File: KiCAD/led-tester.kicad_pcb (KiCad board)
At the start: 2 copper layers, 53.3 x 30.5 mm, 25 parts, among them IC401 ATTINY1634, P101 CONN_01X02, P102 CONN_01X02, P103 CONN_01X03, P104 CONN_02X03, P401 CONN_02X07, SW301 SWITCH_SPDT, U201 LM317L, U301 MCP1702

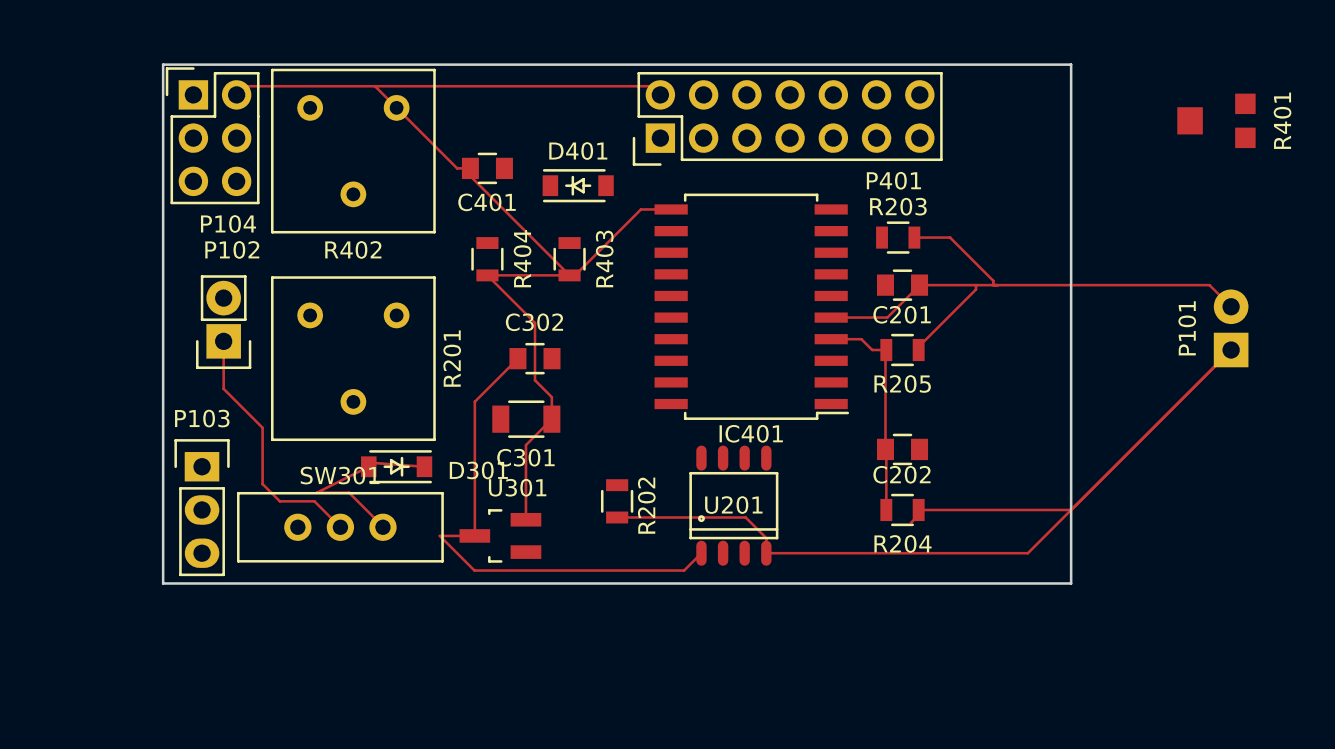
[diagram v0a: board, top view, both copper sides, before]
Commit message: switching back to an ATTiny84 or ATTiny84A
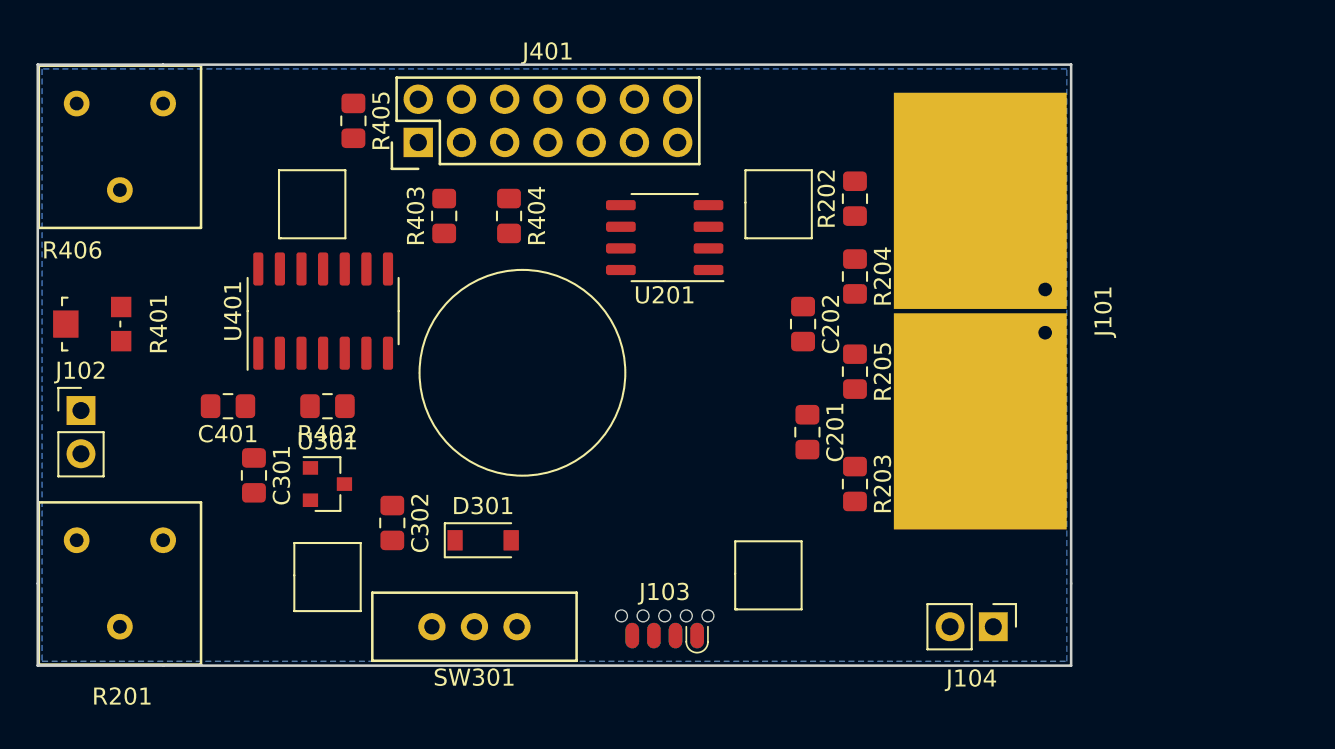
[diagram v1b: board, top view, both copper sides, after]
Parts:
- removed D401: Schottky, Diodes_SMD:SOD-123
- removed IC401: ATTINY1634, led-tester:SOIC-20_7.5x12.8mm_Pitch1.27mm
- removed P101: CONN_01X02, led-tester:LED_touch_pads
- removed P102: CONN_01X02, Pin_Headers:Pin_Header_Straight_1x02
- removed P103: CONN_01X03, Pin_Headers:Pin_Header_Straight_1x03
- removed P104: CONN_02X03, Pin_Headers:Pin_Header_Straight_2x03
- removed P401: CONN_02X07, led-tester:Pololu_diplay_2x07
- added J101: NOPOP, led-tester:LED-LargePads, F.Cu at (153.4, 65.3)
- added J102: NOPOP, Connector_PinHeader_2.54mm:PinHeader_1x02_P2.54mm_Vertical, F.Cu at (96.8, 71.1)
- added J103: Conn_02x04_Counter_Clockwise, led-tester:SOIC_clipProgSmall, F.Cu at (131.1, 85.1)
- added J104: Conn_01x02, Connector_PinHeader_2.54mm:PinHeader_1x02_P2.54mm_Vertical, F.Cu at (150.4, 83.8)
- added J401: Conn_02x07_Odd_Even, led-tester:Pololu_diplay_2x07, F.Cu at (124.2, 54.1)
- added R405: 4.5K, Resistor_SMD:R_0805_2012Metric_Pad1.15x1.40mm_HandSolder, F.Cu at (112.8, 54.1)
- added R406: 10k, led-tester:bourns_3386_potentiometer, F.Cu at (99.1, 55.6)
- added U401: ATtiny84-20SSU, Package_SO:SOIC-14_3.9x8.7mm_P1.27mm, F.Cu at (111.0, 65.3)
- C201, C202, C302, C401: footprint Capacitors_SMD:C_0805 -> Capacitor_SMD:C_0805_2012Metric_Pad1.15x1.40mm_HandSolder
- C301: footprint Capacitors_SMD:C_1206 -> Capacitor_SMD:C_0805_2012Metric_Pad1.15x1.40mm_HandSolder
- D301: footprint Diodes_SMD:SOD-123 -> Diode_SMD:D_SOD-123
- R202, R203, R204, R205: footprint Resistors_SMD:R_0805 -> Resistor_SMD:R_0805_2012Metric_Pad1.15x1.40mm_HandSolder
- R402: value 10k -> 10K; footprint led-tester:bourns_3386_potentiometer -> Resistor_SMD:R_0805_2012Metric_Pad1.15x1.40mm_HandSolder
- R403, R404: value 10K -> 4.5K; footprint Resistors_SMD:R_0805 -> Resistor_SMD:R_0805_2012Metric_Pad1.15x1.40mm_HandSolder
- U201: footprint Power_Integrations:SO-8 -> Package_SO:SO-8_3.9x4.9mm_P1.27mm
- U301: footprint TO_SOT_Packages_SMD:SOT-23_Handsoldering -> Package_TO_SOT_SMD:SOT-23
- moved R401 67.1 mm to (97.5, 66.0)
- moved R202 22.6 mm to (142.2, 58.7)
- moved C401 20.7 mm to (105.4, 70.9), turned to 180 degrees
- moved R201 19.0 mm to (99.1, 81.3)
- moved C301 16.3 mm to (106.9, 74.9), turned to 270 degrees
- moved U201 16.3 mm to (131.1, 61.0), turned to 180 degrees
- moved R402 15.1 mm to (111.3, 70.9), turned to 180 degrees
- moved R203 14.7 mm to (142.2, 75.4), turned to 270 degrees
- moved R204 14.0 mm to (142.2, 63.2), turned to 270 degrees
- moved C302 12.8 mm to (115.1, 77.7), turned to 270 degrees
- moved U301 10.6 mm to (111.3, 75.4), turned to 0 degrees
- moved C201 10.3 mm to (139.4, 72.4), turned to 270 degrees
- moved SW301 9.80 mm to (119.9, 83.8), turned to 0 degrees
- moved C202 9.40 mm to (139.2, 66.0), turned to 270 degrees
- moved R403 7.79 mm to (118.1, 59.7), turned to 90 degrees
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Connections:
- R201 pad 1: Net-(R201-Pad1) -> (no net)
- R402 pad 1: GND -> /Digital Display/RESET
- R402 pad 2: Net-(IC401-Pad3) -> +5V
- R403 pad 1: /Digital Display/RESET -> /Digital Display/MOSI
- R403 pad 2: +5V -> /Digital Display/a4
- R404 pad 1: Net-(D401-Pad2) -> /Digital Display/a5
- R404 pad 2: +5V -> /Digital Display/MISO
- SW301 pad 1: Net-(D301-Pad2) -> /power/Battery+
- SW301 pad 2: /power/Battery+ -> Net-(D301-Pad2)
- SW301 pad 3: Net-(SW301-Pad3) -> (no net)
- U201 pad 3: Net-(U201-Pad3) -> Net-(R201-Pad2)
- U201 pad 5: Net-(U201-Pad5) -> (no net)
- U201 pad 6: Net-(U201-Pad6) -> Net-(R201-Pad2)
- U201 pad 7: Net-(U201-Pad7) -> Net-(R201-Pad2)
- U201 pad 8: Net-(U201-Pad8) -> (no net)
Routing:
- net +5V: track 70.6 -> 0.00 mm
- net /current_sensor/LED+: track 64.9 -> 0.00 mm
- net /current_sensor/LED-: track 37.2 -> 0.00 mm
- net +9V: track 30.1 -> 0.00 mm
- net /power/Battery+: track 15.0 -> 0.00 mm
- net /Digital Display/LEDhigh: track 12.9 -> 0.00 mm
- net Net-(D301-Pad2): track 11.6 -> 0.00 mm
- added copper zone on B.Cu, net GND
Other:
- board size 53.3 x 30.5 mm -> 60.7 x 35.3 mm

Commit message: Regenerated the netlist
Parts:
- removed J104: Conn_01x02, Connector_PinHeader_2.54mm:PinHeader_1x02_P2.54mm_Vertical
- U401: value ATtiny84-20SSU -> ATtiny84A-SSU
- moved J103 18.9 mm to (150.0, 85.1)
- moved U201 10.2 mm to (133.6, 70.9), turned to 270 degrees
- moved J102 1.48 mm to (97.5, 72.4), turned to 90 degrees
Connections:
- J103 pad 3: (no net) -> /Digital Display/TX
- J401 pad 4: /Digital Display/a4 -> /Digital Display/RS
- J401 pad 5: /Digital Display/a5 -> /Digital Display/RW
- J401 pad 6: /Digital Display/a6 -> /Digital Display/CE
- R403 pad 2: /Digital Display/a4 -> /Digital Display/a13
- R404 pad 1: /Digital Display/a5 -> /Digital Display/a12
- R405 pad 1: /Digital Display/a6 -> /Digital Display/a11
- U401 pad 10: /Digital Display/a14 -> /Digital Display/CE
- U401 pad 11: /Digital Display/a13 -> /Digital Display/LEDhigh
- U401 pad 12: /Digital Display/a12 -> /current_sensor/LED-
- U401 pad 13: /Digital Display/a11 -> Net-(R406-Pad2)
- U401 pad 2: /Digital Display/LEDhigh -> /Digital Display/RS
- U401 pad 3: /current_sensor/LED- -> /Digital Display/RW
- U401 pad 6: Net-(R406-Pad2) -> /Digital Display/a14
